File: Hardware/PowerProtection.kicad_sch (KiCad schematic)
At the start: 17 parts, among them IC4 LM76202QPWPRQ1

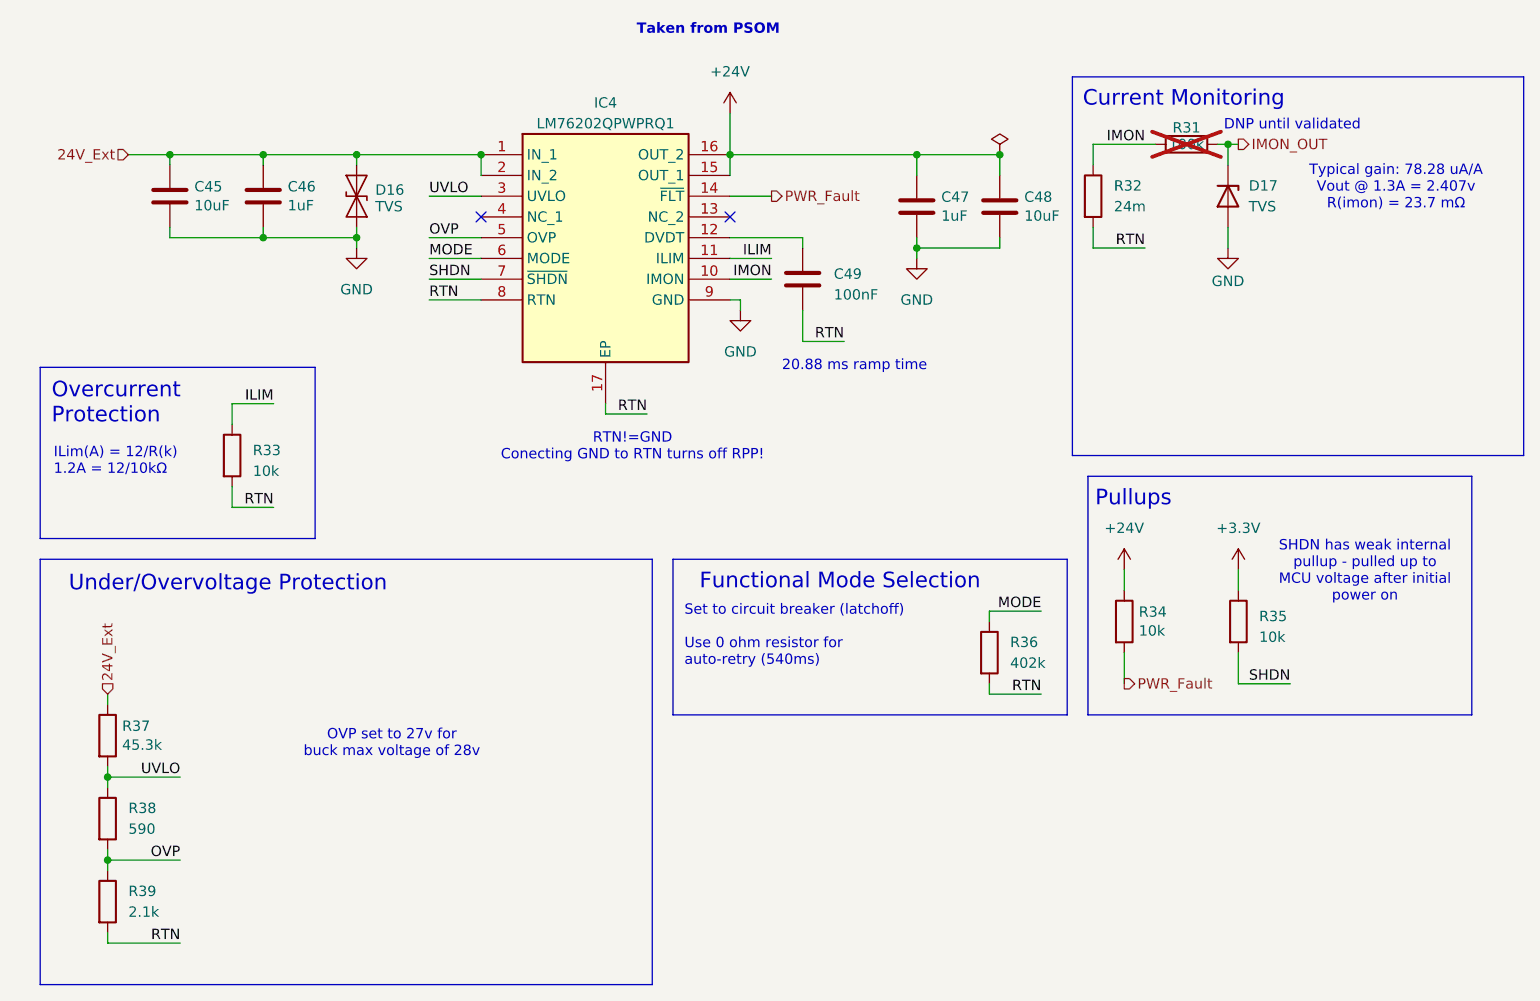
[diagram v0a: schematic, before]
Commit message: added voltage reference, shunt model; addressed comments
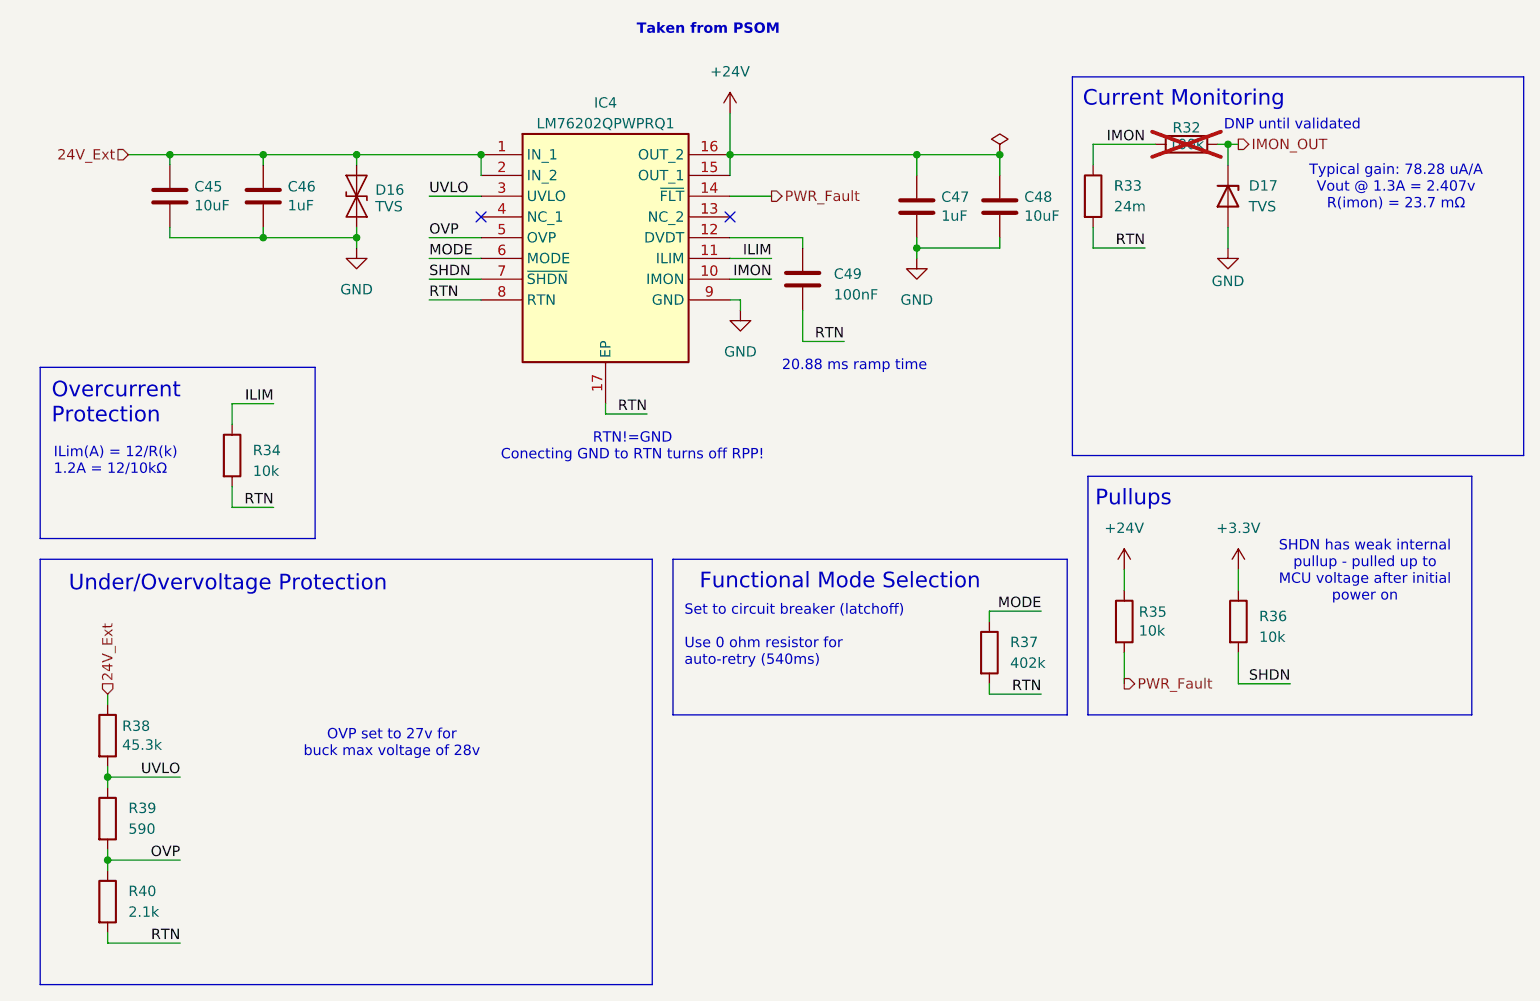
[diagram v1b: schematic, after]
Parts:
- renumbered R31 to R32, R32 to R33, R33 to R34, R34 to R35, R35 to R36, R36 to R37, R37 to R38, R38 to R39, R39 to R40
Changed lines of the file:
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@@
 		(dnp no)
 		(fields_autoplaced yes)
-		(property "Reference" "#PWR0115"
+		(property "Reference" "#PWR0116"
 			(at 52.07 49.53 0)
 			(effects
@@
 			(project "BPS-AmperesPCB"
 				(path "/a452d214-ea00-440d-a445-5d6103fda43a/3b2a70f8-48f8-45b9-b0fe-085893d574c0/bd9a5644-5430-4918-ab28-771dd7faeab6"
-					(reference "#PWR0115")
+					(reference "#PWR0116")
 					(unit 1)
 				)
@@
 		(on_board yes)
 		(dnp no)
-		(property "Reference" "R37"
+		(property "Reference" "R38"
 			(at 23.368 101.7016 0)
 			(effects
@@
 			(project "BPS-AmperesPCB"
 				(path "/a452d214-ea00-440d-a445-5d6103fda43a/3b2a70f8-48f8-45b9-b0fe-085893d574c0/bd9a5644-5430-4918-ab28-771dd7faeab6"
-					(reference "R37")
+					(reference "R38")
 					(unit 1)
 				)
@@
 		(dnp no)
 		(fields_autoplaced yes)
-		(property "Reference" "R39"
+		(property "Reference" "R40"
 			(at 24.13 121.9199 0)
 			(effects
@@
 			(project "BPS-AmperesPCB"
 				(path "/a452d214-ea00-440d-a445-5d6103fda43a/3b2a70f8-48f8-45b9-b0fe-085893d574c0/bd9a5644-5430-4918-ab28-771dd7faeab6"
-					(reference "R39")
+					(reference "R40")
 					(unit 1)
 				)
@@
 		(dnp no)
 		(fields_autoplaced yes)
-		(property "Reference" "R32"
+		(property "Reference" "R33"
 			(at 144.78 35.5599 0)
 			(effects
@@
 			(project "BPS-AmperesPCB"
 				(path "/a452d214-ea00-440d-a445-5d6103fda43a/3b2a70f8-48f8-45b9-b0fe-085893d574c0/bd9a5644-5430-4918-ab28-771dd7faeab6"
-					(reference "R32")
+					(reference "R33")
 					(unit 1)
 				)
@@
 		(on_board yes)
 		(dnp no)
-		(property "Reference" "#FLG09"
+		(property "Reference" "#FLG07"
 			(at 130.81 29.845 0)
 			(effects
@@
 			(project "BPS-AmperesPCB"
 				(path "/a452d214-ea00-440d-a445-5d6103fda43a/3b2a70f8-48f8-45b9-b0fe-085893d574c0/bd9a5644-5430-4918-ab28-771dd7faeab6"
-					(reference "#FLG09")
+					(reference "#FLG07")
 					(unit 1)
 				)
@@
 		(dnp no)
 		(fields_autoplaced yes)
-		(property "Reference" "R33"
+		(property "Reference" "R34"
 			(at 39.37 67.945 0)
 			(effects
@@
 			(project "BPS-AmperesPCB"
 				(path "/a452d214-ea00-440d-a445-5d6103fda43a/3b2a70f8-48f8-45b9-b0fe-085893d574c0/bd9a5644-5430-4918-ab28-771dd7faeab6"
-					(reference "R33")
+					(reference "R34")
 					(unit 1)
 				)
@@
 		(dnp no)
 		(fields_autoplaced yes)
-		(property "Reference" "R36"
+		(property "Reference" "R37"
 			(at 132.08 91.4399 0)
 			(effects
@@
 			(project "BPS-AmperesPCB"
 				(path "/a452d214-ea00-440d-a445-5d6103fda43a/3b2a70f8-48f8-45b9-b0fe-085893d574c0/bd9a5644-5430-4918-ab28-771dd7faeab6"
-					(reference "R36")
+					(reference "R37")
 					(unit 1)
 				)
@@
 		(dnp no)
 		(fields_autoplaced yes)
-		(property "Reference" "#PWR0117"
+		(property "Reference" "#PWR0118"
 			(at 120.65 50.8 0)
 			(effects
@@
 			(project "BPS-AmperesPCB"
 				(path "/a452d214-ea00-440d-a445-5d6103fda43a/3b2a70f8-48f8-45b9-b0fe-085893d574c0/bd9a5644-5430-4918-ab28-771dd7faeab6"
-					(reference "#PWR0117")
+					(reference "#PWR0118")
 					(unit 1)
 				)
@@
 		(on_board yes)
 		(dnp yes)
-		(property "Reference" "R31"
+		(property "Reference" "R32"
 			(at 153.67 28.448 90)
 			(effects
@@
 			(project "BPS-AmperesPCB"
 				(path "/a452d214-ea00-440d-a445-5d6103fda43a/3b2a70f8-48f8-45b9-b0fe-085893d574c0/bd9a5644-5430-4918-ab28-771dd7faeab6"
-					(reference "R31")
+					(reference "R32")
 					(unit 1)
 				)
@@
 		(dnp no)
 		(fields_autoplaced yes)
-		(property "Reference" "#PWR0118"
+		(property "Reference" "#PWR0119"
 			(at 99.06 57.15 0)
 			(effects
@@
 			(project "BPS-AmperesPCB"
 				(path "/a452d214-ea00-440d-a445-5d6103fda43a/3b2a70f8-48f8-45b9-b0fe-085893d574c0/bd9a5644-5430-4918-ab28-771dd7faeab6"
-					(reference "#PWR0118")
+					(reference "#PWR0119")
 					(unit 1)
 				)
@@
 		(dnp no)
 		(fields_autoplaced yes)
-		(property "Reference" "#PWR0114"
+		(property "Reference" "#PWR0115"
 			(at 97.79 30.48 0)
 			(effects
@@
 			(project "BPS-AmperesPCB"
 				(path "/a452d214-ea00-440d-a445-5d6103fda43a/3b2a70f8-48f8-45b9-b0fe-085893d574c0/bd9a5644-5430-4918-ab28-771dd7faeab6"
-					(reference "#PWR0114")
+					(reference "#PWR0115")
 					(unit 1)
 				)
@@
 		(on_board yes)
 		(dnp no)
-		(property "Reference" "R34"
+		(property "Reference" "R35"
 			(at 147.828 87.7316 0)
 			(effects
@@
 			(project "BPS-AmperesPCB"
 				(path "/a452d214-ea00-440d-a445-5d6103fda43a/3b2a70f8-48f8-45b9-b0fe-085893d574c0/bd9a5644-5430-4918-ab28-771dd7faeab6"
-					(reference "R34")
+					(reference "R35")
 					(unit 1)
 				)
@@
 		(dnp no)
 		(fields_autoplaced yes)
-		(property "Reference" "R38"
+		(property "Reference" "R39"
 			(at 24.13 111.7599 0)
 			(effects
@@
 			(project "BPS-AmperesPCB"
 				(path "/a452d214-ea00-440d-a445-5d6103fda43a/3b2a70f8-48f8-45b9-b0fe-085893d574c0/bd9a5644-5430-4918-ab28-771dd7faeab6"
-					(reference "R38")
+					(reference "R39")
 					(unit 1)
 				)
@@
 		(dnp no)
 		(fields_autoplaced yes)
-		(property "Reference" "#PWR0120"
+		(property "Reference" "#PWR0121"
 			(at 160.02 86.36 0)
 			(effects
@@
 			(project "BPS-AmperesPCB"
 				(path "/a452d214-ea00-440d-a445-5d6103fda43a/3b2a70f8-48f8-45b9-b0fe-085893d574c0/bd9a5644-5430-4918-ab28-771dd7faeab6"
-					(reference "#PWR0120")
+					(reference "#PWR0121")
 					(unit 1)
 				)
@@
 		(dnp no)
 		(fields_autoplaced yes)
-		(property "Reference" "#PWR0119"
+		(property "Reference" "#PWR0120"
 			(at 146.05 86.36 0)
 			(effects
@@
 			(project "BPS-AmperesPCB"
 				(path "/a452d214-ea00-440d-a445-5d6103fda43a/3b2a70f8-48f8-45b9-b0fe-085893d574c0/bd9a5644-5430-4918-ab28-771dd7faeab6"
-					(reference "#PWR0119")
+					(reference "#PWR0120")
 					(unit 1)
 				)
@@
 		(dnp no)
 		(fields_autoplaced yes)
-		(property "Reference" "R35"
+		(property "Reference" "R36"
 			(at 162.56 88.265 0)
 			(effects
@@
 			(project "BPS-AmperesPCB"
 				(path "/a452d214-ea00-440d-a445-5d6103fda43a/3b2a70f8-48f8-45b9-b0fe-085893d574c0/bd9a5644-5430-4918-ab28-771dd7faeab6"
-					(reference "R35")
+					(reference "R36")
 					(unit 1)
 				)
@@
 		(on_board yes)
 		(dnp no)
-		(property "Reference" "#PWR0116"
+		(property "Reference" "#PWR0117"
 			(at 158.75 49.53 0)
 			(effects
@@
 			(project "BPS-AmperesPCB"
 				(path "/a452d214-ea00-440d-a445-5d6103fda43a/3b2a70f8-48f8-45b9-b0fe-085893d574c0/bd9a5644-5430-4918-ab28-771dd7faeab6"
-					(reference "#PWR0116")
-					(unit 1)
-				)
+					(reference "#PWR0117")
+					(unit 1)
+				)

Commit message: lay out lay out
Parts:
- renumbered C45 to C50, C46 to C51, C47 to C52, C48 to C53, C49 to C54, D16 to D17, D17 to D18, IC4 to IC5, R32 to R30, R33 to R31, R34 to R32, R35 to R33, R36 to R34, R37 to R35, R38 to R36, R39 to R37, R40 to R38
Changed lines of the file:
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@@
 		(effects
 			(font
-				(size 1.27 1.27)
+				(size 1.524 1.524)
 				(thickness 0.254)
 				(bold yes)
@@
 		(dnp no)
 		(fields_autoplaced yes)
-		(property "Reference" "C49"
+		(property "Reference" "C54"
 			(at 110.49 46.355 0)
 			(effects
@@
 			(project "BPS-AmperesPCB"
 				(path "/a452d214-ea00-440d-a445-5d6103fda43a/3b2a70f8-48f8-45b9-b0fe-085893d574c0/bd9a5644-5430-4918-ab28-771dd7faeab6"
-					(reference "C49")
+					(reference "C54")
 					(unit 1)
 				)
@@
 		(dnp no)
 		(fields_autoplaced yes)
-		(property "Reference" "#PWR0116"
+		(property "Reference" "#PWR0119"
 			(at 52.07 49.53 0)
 			(effects
@@
 			(project "BPS-AmperesPCB"
 				(path "/a452d214-ea00-440d-a445-5d6103fda43a/3b2a70f8-48f8-45b9-b0fe-085893d574c0/bd9a5644-5430-4918-ab28-771dd7faeab6"
-					(reference "#PWR0116")
+					(reference "#PWR0119")
 					(unit 1)
 				)
@@
 		(on_board yes)
 		(dnp no)
-		(property "Reference" "R38"
+		(property "Reference" "R36"
 			(at 23.368 101.7016 0)
 			(effects
@@
 			(project "BPS-AmperesPCB"
 				(path "/a452d214-ea00-440d-a445-5d6103fda43a/3b2a70f8-48f8-45b9-b0fe-085893d574c0/bd9a5644-5430-4918-ab28-771dd7faeab6"
-					(reference "R38")
+					(reference "R36")
 					(unit 1)
 				)
@@
 		(dnp no)
 		(fields_autoplaced yes)
-		(property "Reference" "R40"
+		(property "Reference" "R38"
 			(at 24.13 121.9199 0)
 			(effects
@@
 			(project "BPS-AmperesPCB"
 				(path "/a452d214-ea00-440d-a445-5d6103fda43a/3b2a70f8-48f8-45b9-b0fe-085893d574c0/bd9a5644-5430-4918-ab28-771dd7faeab6"
-					(reference "R40")
+					(reference "R38")
 					(unit 1)
 				)
@@
 		(on_board yes)
 		(dnp no)
-		(property "Reference" "C45"
+		(property "Reference" "C50"
 			(at 32.2072 35.6616 0)
 			(effects
@@
 			(project "BPS-AmperesPCB"
 				(path "/a452d214-ea00-440d-a445-5d6103fda43a/3b2a70f8-48f8-45b9-b0fe-085893d574c0/bd9a5644-5430-4918-ab28-771dd7faeab6"
-					(reference "C45")
+					(reference "C50")
 					(unit 1)
 				)
@@
 		(dnp no)
 		(fields_autoplaced yes)
-		(property "Reference" "IC4"
+		(property "Reference" "IC5"
 			(at 82.55 25.4 0)
 			(effects
@@
 			(project ""
 				(path "/a452d214-ea00-440d-a445-5d6103fda43a/3b2a70f8-48f8-45b9-b0fe-085893d574c0/bd9a5644-5430-4918-ab28-771dd7faeab6"
-					(reference "IC4")
+					(reference "IC5")
 					(unit 1)
 				)
@@
 		(dnp no)
 		(fields_autoplaced yes)
-		(property "Reference" "R33"
+		(property "Reference" "R31"
 			(at 144.78 35.5599 0)
 			(effects
@@
 			(project "BPS-AmperesPCB"
 				(path "/a452d214-ea00-440d-a445-5d6103fda43a/3b2a70f8-48f8-45b9-b0fe-085893d574c0/bd9a5644-5430-4918-ab28-771dd7faeab6"
-					(reference "R33")
+					(reference "R31")
 					(unit 1)
 				)
@@
 		(dnp no)
 		(fields_autoplaced yes)
-		(property "Reference" "R34"
+		(property "Reference" "R32"
 			(at 39.37 67.945 0)
 			(effects
@@
 			(project "BPS-AmperesPCB"
 				(path "/a452d214-ea00-440d-a445-5d6103fda43a/3b2a70f8-48f8-45b9-b0fe-085893d574c0/bd9a5644-5430-4918-ab28-771dd7faeab6"
-					(reference "R34")
+					(reference "R32")
 					(unit 1)
 				)
@@
 		(dnp no)
 		(fields_autoplaced yes)
-		(property "Reference" "R37"
+		(property "Reference" "R35"
 			(at 132.08 91.4399 0)
 			(effects
@@
 			(project "BPS-AmperesPCB"
 				(path "/a452d214-ea00-440d-a445-5d6103fda43a/3b2a70f8-48f8-45b9-b0fe-085893d574c0/bd9a5644-5430-4918-ab28-771dd7faeab6"
-					(reference "R37")
+					(reference "R35")
 					(unit 1)
 				)
@@
 		(dnp no)
 		(fields_autoplaced yes)
-		(property "Reference" "#PWR0118"
+		(property "Reference" "#PWR0121"
 			(at 120.65 50.8 0)
 			(effects
@@
 			(project "BPS-AmperesPCB"
 				(path "/a452d214-ea00-440d-a445-5d6103fda43a/3b2a70f8-48f8-45b9-b0fe-085893d574c0/bd9a5644-5430-4918-ab28-771dd7faeab6"
-					(reference "#PWR0118")
+					(reference "#PWR0121")
 					(unit 1)
 				)
@@
 		(on_board yes)
 		(dnp yes)
-		(property "Reference" "R32"
+		(property "Reference" "R30"
 			(at 153.67 28.448 90)
 			(effects
@@
 			(project "BPS-AmperesPCB"
 				(path "/a452d214-ea00-440d-a445-5d6103fda43a/3b2a70f8-48f8-45b9-b0fe-085893d574c0/bd9a5644-5430-4918-ab28-771dd7faeab6"
-					(reference "R32")
+					(reference "R30")
 					(unit 1)
 				)
@@
 		(dnp no)
 		(fields_autoplaced yes)
-		(property "Reference" "#PWR0119"
+		(property "Reference" "#PWR0122"
 			(at 99.06 57.15 0)
 			(effects
@@
 			(project "BPS-AmperesPCB"
 				(path "/a452d214-ea00-440d-a445-5d6103fda43a/3b2a70f8-48f8-45b9-b0fe-085893d574c0/bd9a5644-5430-4918-ab28-771dd7faeab6"
-					(reference "#PWR0119")
+					(reference "#PWR0122")
 					(unit 1)
 				)
@@
 		(dnp no)
 		(fields_autoplaced yes)
-		(property "Reference" "#PWR0115"
+		(property "Reference" "#PWR0118"
 			(at 97.79 30.48 0)
 			(effects
@@
 			(project "BPS-AmperesPCB"
 				(path "/a452d214-ea00-440d-a445-5d6103fda43a/3b2a70f8-48f8-45b9-b0fe-085893d574c0/bd9a5644-5430-4918-ab28-771dd7faeab6"
-					(reference "#PWR0115")
+					(reference "#PWR0118")
 					(unit 1)
 				)
@@
 		(on_board yes)
 		(dnp no)
-		(property "Reference" "R35"
+		(property "Reference" "R33"
 			(at 147.828 87.7316 0)
 			(effects
@@
 			(project "BPS-AmperesPCB"
 				(path "/a452d214-ea00-440d-a445-5d6103fda43a/3b2a70f8-48f8-45b9-b0fe-085893d574c0/bd9a5644-5430-4918-ab28-771dd7faeab6"
-					(reference "R35")
+					(reference "R33")
 					(unit 1)
 				)
@@
 		(on_board yes)
 		(dnp no)
-		(property "Reference" "C48"
+		(property "Reference" "C53"
 			(at 133.8072 36.9316 0)
 			(effects
@@
 			(project "BPS-AmperesPCB"
 				(path "/a452d214-ea00-440d-a445-5d6103fda43a/3b2a70f8-48f8-45b9-b0fe-085893d574c0/bd9a5644-5430-4918-ab28-771dd7faeab6"
-					(reference "C48")
+					(reference "C53")
 					(unit 1)
 				)
@@
 		(dnp no)
 		(fields_autoplaced yes)
-		(property "Reference" "R39"
+		(property "Reference" "R37"
 			(at 24.13 111.7599 0)
 			(effects
@@
 			(project "BPS-AmperesPCB"
 				(path "/a452d214-ea00-440d-a445-5d6103fda43a/3b2a70f8-48f8-45b9-b0fe-085893d574c0/bd9a5644-5430-4918-ab28-771dd7faeab6"
-					(reference "R39")
+					(reference "R37")
 					(unit 1)
 				)
@@
 		(dnp no)
 		(fields_autoplaced yes)
-		(property "Reference" "#PWR0121"
+		(property "Reference" "#PWR0124"
 			(at 160.02 86.36 0)
 			(effects
@@
 			(project "BPS-AmperesPCB"
 				(path "/a452d214-ea00-440d-a445-5d6103fda43a/3b2a70f8-48f8-45b9-b0fe-085893d574c0/bd9a5644-5430-4918-ab28-771dd7faeab6"
-					(reference "#PWR0121")
+					(reference "#PWR0124")
 					(unit 1)
 				)
@@
 		(dnp no)
 		(fields_autoplaced yes)
-		(property "Reference" "#PWR0120"
+		(property "Reference" "#PWR0123"
 			(at 146.05 86.36 0)
 			(effects
@@
 			(project "BPS-AmperesPCB"
 				(path "/a452d214-ea00-440d-a445-5d6103fda43a/3b2a70f8-48f8-45b9-b0fe-085893d574c0/bd9a5644-5430-4918-ab28-771dd7faeab6"
-					(reference "#PWR0120")
+					(reference "#PWR0123")
 					(unit 1)
 				)
@@
 		(on_board yes)
 		(dnp no)
-		(property "Reference" "D16"
+		(property "Reference" "D17"
 			(at 54.356 36.068 90)
 			(effects
@@
 			(project "BPS-AmperesPCB"
 				(path "/a452d214-ea00-440d-a445-5d6103fda43a/3b2a70f8-48f8-45b9-b0fe-085893d574c0/bd9a5644-5430-4918-ab28-771dd7faeab6"
-					(reference "D16")
+					(reference "D17")
 					(unit 1)
 				)
@@
 		(dnp no)
 		(fields_autoplaced yes)
-		(property "Reference" "R36"
+		(property "Reference" "R34"
 			(at 162.56 88.265 0)
 			(effects
@@
 			(project "BPS-AmperesPCB"
 				(path "/a452d214-ea00-440d-a445-5d6103fda43a/3b2a70f8-48f8-45b9-b0fe-085893d574c0/bd9a5644-5430-4918-ab28-771dd7faeab6"
-					(reference "R36")
+					(reference "R34")
 					(unit 1)
 				)
@@
 		(dnp no)
 		(fields_autoplaced yes)
-		(property "Reference" "D17"
+		(property "Reference" "D18"
 			(at 161.29 35.5599 90)
 			(effects
@@
 			(project "BPS-AmperesPCB"
 				(path "/a452d214-ea00-440d-a445-5d6103fda43a/3b2a70f8-48f8-45b9-b0fe-085893d574c0/bd9a5644-5430-4918-ab28-771dd7faeab6"
-					(reference "D17")
+					(reference "D18")
 					(unit 1)
 				)
@@
 		(on_board yes)
 		(dnp no)
-		(property "Reference" "C47"
+		(property "Reference" "C52"
 			(at 123.6472 36.9316 0)
 			(effects
@@
 			(project "BPS-AmperesPCB"
 				(path "/a452d214-ea00-440d-a445-5d6103fda43a/3b2a70f8-48f8-45b9-b0fe-085893d574c0/bd9a5644-5430-4918-ab28-771dd7faeab6"
-					(reference "C47")
+					(reference "C52")
 					(unit 1)
 				)
@@
 		(on_board yes)
 		(dnp no)
-		(property "Reference" "C46"
+		(property "Reference" "C51"
 			(at 43.6372 35.6616 0)
 			(effects
@@
 			(project "BPS-AmperesPCB"
 				(path "/a452d214-ea00-440d-a445-5d6103fda43a/3b2a70f8-48f8-45b9-b0fe-085893d574c0/bd9a5644-5430-4918-ab28-771dd7faeab6"
-					(reference "C46")
+					(reference "C51")
 					(unit 1)
 				)
@@
 		(on_board yes)
 		(dnp no)
-		(property "Reference" "#PWR0117"
+		(property "Reference" "#PWR0120"
 			(at 158.75 49.53 0)
 			(effects
@@
 			(project "BPS-AmperesPCB"
 				(path "/a452d214-ea00-440d-a445-5d6103fda43a/3b2a70f8-48f8-45b9-b0fe-085893d574c0/bd9a5644-5430-4918-ab28-771dd7faeab6"
-					(reference "#PWR0117")
+					(reference "#PWR0120")
 					(unit 1)
 				)

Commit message: silkscreen work
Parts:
- R31: value 24m -> 19K
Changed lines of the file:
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@@
 			)
 		)
-		(property "Value" "24m"
+		(property "Value" "19K"
 			(at 144.78 38.0999 0)
 			(effects
